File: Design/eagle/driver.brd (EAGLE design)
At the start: 50 x 50 mm, 44 parts, among them IC1 V_REG_LD1117VXX, Q1 600mA/40V, Q10 600mA/40V, Q11 600mA/40V, Q13 600mA/40V, Q14 600mA/40V, Q15 600mA/40V, Q2 600mA/40V, Q3 600mA/40V, Q5 600mA/40V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

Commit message: Correcciones al PCB
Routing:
- net VCC: vias 6 -> 7
- net GND: vias 8 -> 9
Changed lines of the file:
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@@
 <wire x1="15.356" y1="28.956" x2="15.356" y2="25.908" width="0.4064" layer="16"/>
 <wire x1="17.018" y1="44.958" x2="15.748" y2="43.688" width="1.27" layer="16"/>
+<via x="22.9" y="40.64" extent="1-16" drill="0.6" shape="square"/>
 </signal>
 <signal name="N$1">
@@
 <wire x1="25.654" y1="35.56" x2="22.9" y2="35.56" width="1.27" layer="16"/>
 <wire x1="22.9" y1="35.56" x2="22.86" y2="35.6" width="1.27" layer="16"/>
-<wire x1="22.86" y1="35.6" x2="12.486" y2="35.6" width="1.27" layer="16"/>
 <wire x1="12.486" y1="35.6" x2="11.43" y2="34.544" width="1.27" layer="16"/>
 <wire x1="25.654" y1="37.454" x2="25.654" y2="35.56" width="0.6096" layer="16"/>
@@
 <vertex x="44.958" y="11.938"/>
 </polygon>
+<via x="22.9" y="35.56" extent="1-16" drill="0.6" shape="square"/>
+<wire x1="22.86" y1="35.6" x2="12.486" y2="35.6" width="1.27" layer="16"/>
 </signal>
 <signal name="M1T">

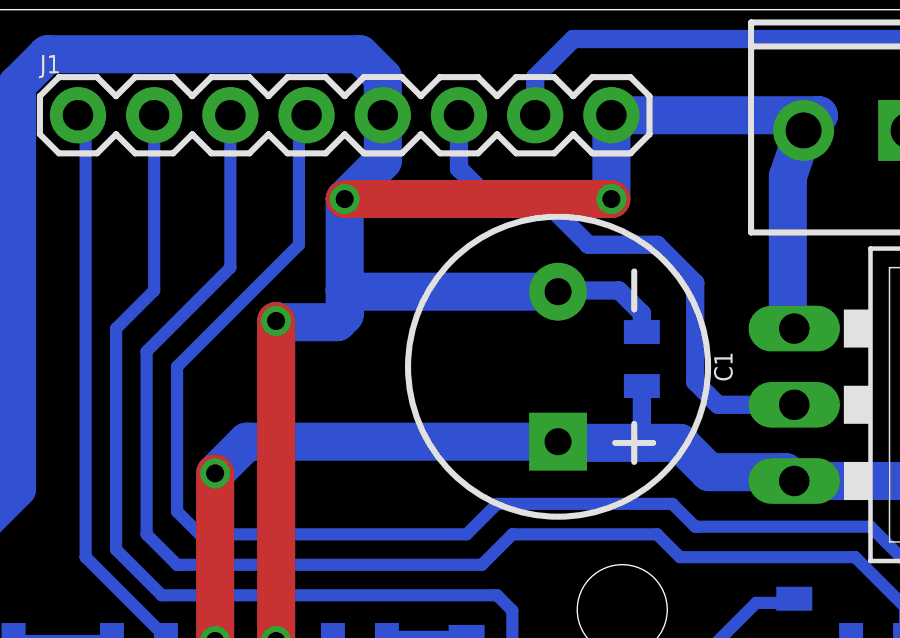
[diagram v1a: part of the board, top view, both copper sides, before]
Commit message: Removidos vias sobrepuestos automaticamente.
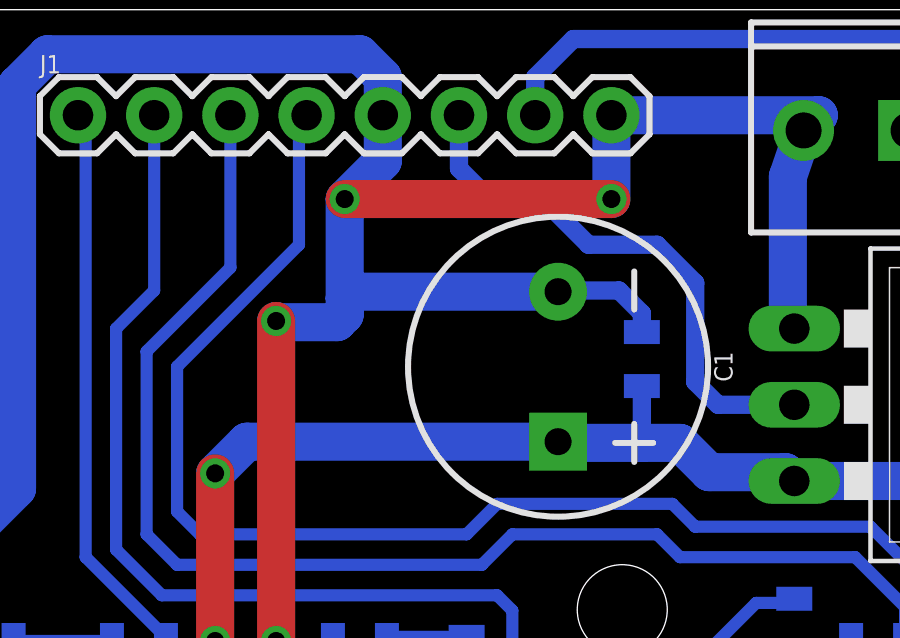
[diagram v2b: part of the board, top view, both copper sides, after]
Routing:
- net GND: track 240.8 -> 241.0 mm, vias 9 -> 8
- net VCC: vias 7 -> 6
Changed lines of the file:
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@@
 <wire x1="24.638" y1="43.688" x2="15.748" y2="43.688" width="1.27" layer="1"/>
 <via x="15.748" y="43.688" extent="1-16" drill="0.6"/>
-<wire x1="15.748" y1="43.688" x2="15.748" y2="40.64" width="1.27" layer="16"/>
-<wire x1="15.748" y1="40.64" x2="15.748" y2="39.838" width="1.27" layer="16"/>
+<wire x1="15.748" y1="43.688" x2="15.748" y2="40.386" width="1.27" layer="16"/>
+<wire x1="15.748" y1="40.386" x2="15.748" y2="39.838" width="1.27" layer="16"/>
 <wire x1="15.748" y1="39.838" x2="15.494" y2="39.584" width="1.27" layer="16"/>
 <wire x1="13.462" y1="17.272" x2="13.462" y2="11.938" width="1.27" layer="16"/>
@@
 <wire x1="25.908" y1="10.922" x2="25.908" y2="11.938" width="1.27" layer="16"/>
 <wire x1="22.86" y1="40.6" x2="15.788" y2="40.6" width="1.27" layer="16"/>
-<wire x1="15.788" y1="40.6" x2="15.748" y2="40.64" width="1.27" layer="16"/>
+<wire x1="15.788" y1="40.6" x2="15.748" y2="40.386" width="1.27" layer="16"/>
 <wire x1="27.548" y1="25.908" x2="27.548" y2="28.31" width="0.4064" layer="16"/>
 <wire x1="27.548" y1="28.31" x2="29.464" y2="30.226" width="0.4064" layer="16"/>
@@
 <wire x1="15.356" y1="28.956" x2="15.356" y2="25.908" width="0.4064" layer="16"/>
 <wire x1="17.018" y1="44.958" x2="15.748" y2="43.688" width="1.27" layer="16"/>
-<via x="22.9" y="40.64" extent="1-16" drill="0.6" shape="square"/>
 </signal>
 <signal name="N$1">
@@
 <vertex x="44.958" y="11.938"/>
 </polygon>
-<via x="22.9" y="35.56" extent="1-16" drill="0.6" shape="square"/>
 <wire x1="22.86" y1="35.6" x2="12.486" y2="35.6" width="1.27" layer="16"/>
 </signal>

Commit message: Agregados ajustes en PCB para fotosensibilizada.
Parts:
- moved R2 1.78 mm to (7.11, 29.0), turned to 90 degrees
- moved C1 0.51 mm to (22.4, 38.1)
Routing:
- net VCC: track 223.4 -> 225.0 mm
- net A1: track 18.7 -> 17.5 mm
- net GND: track 241.0 -> 242.2 mm
- net B1: track 32.9 -> 34.0 mm
- net A2: track 43.4 -> 44.5 mm
- net B2: track 54.6 -> 55.7 mm
- net N$1: track 12.3 -> 11.8 mm

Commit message: Agregadas correcciones en PCB
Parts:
- C1: value 1mF -> 1000uF
- C2: value 1.0uF -> 10uF
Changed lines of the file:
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@@
 <attribute name="PROD_ID" value=" " x="16.256" y="25.908" size="1.778" layer="28" rot="MR0" display="off"/>
 </element>
-<element name="C1" library="SparkFun-Capacitors" package="CPOL-RADIAL-5MM-10MM" value="1mF" x="22.352" y="38.1" rot="R270">
+<element name="C1" library="SparkFun-Capacitors" package="CPOL-RADIAL-5MM-10MM" value="1000uF" x="22.352" y="38.1" rot="R270">
 <attribute name="PROD_ID" value="CAP-09538" x="22.352" y="38.1" size="1.778" layer="27" rot="R270" display="off"/>
 </element>
-<element name="C2" library="SparkFun-Capacitors" package="0805" value="1.0uF" x="25.654" y="38.354" rot="MR90">
+<element name="C2" library="SparkFun-Capacitors" package="0805" value="10uF" x="25.654" y="38.354" rot="MR90">
 <attribute name="PROD_ID" value="CAP-08064" x="25.654" y="38.354" size="1.778" layer="28" rot="MR90" display="off"/>
 </element>
@@
 <wire x1="24.638" y1="43.434" x2="20.828" y2="43.434" width="0.6096" layer="16"/>
 </signal>
+<signal name="N$17">
+<via x="3.5" y="3.5" extent="1-16" drill="0.7874"/>
+<via x="46.5" y="3.5" extent="1-16" drill="0.7874"/>
+<via x="25" y="30" extent="1-16" drill="0.7874"/>
+<via x="45.72" y="36.858" extent="1-16" drill="0.7874"/>
+<wire x1="25" y1="30" x2="45.72" y2="36.858" width="0" layer="19" extent="1-1"/>
+<wire x1="46.5" y1="3.5" x2="45.72" y2="36.858" width="0" layer="19" extent="1-1"/>
+<wire x1="3.5" y1="3.5" x2="25" y2="30" width="0" layer="19" extent="1-1"/>
+</signal>
 </signals>
